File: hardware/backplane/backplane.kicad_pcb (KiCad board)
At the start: 4 copper layers, 192 x 31.5 mm, 83 parts, among them J1 Bus_PCI_Express_x1, J2 PWR, J3 Bus_PCI_Express_x1, J4 Bus_PCI_Express_x1, J5 Bus_PCI_Express_x1, J6 Bus_PCI_Express_x1, J7 Bus_PCI_Express_x1, J8 Bus_PCI_Express_x1, M1 FAN1, Q1 IRFS7530TRL7PP, Q2 AO3400A, U1 TPS5430DDA, U2 TCA9548APWR, U3 TCA9539PWR, U4 LM74700

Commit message: chore(backplane): fix 3d models
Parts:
- D10, D5, D6, D7, D8, D9: footprint LED_SMD:LED_WS2812B-2020_PLCC4_2.0x2.0mm -> Local Library:LED_WS2812B-2020_PLCC4_2.0x2.0mm

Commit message: chore: assembly cleanup
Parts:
- D10, D5, D6, D7, D8, D9: value WS2812C-2020 -> WS2812C-2020-V6

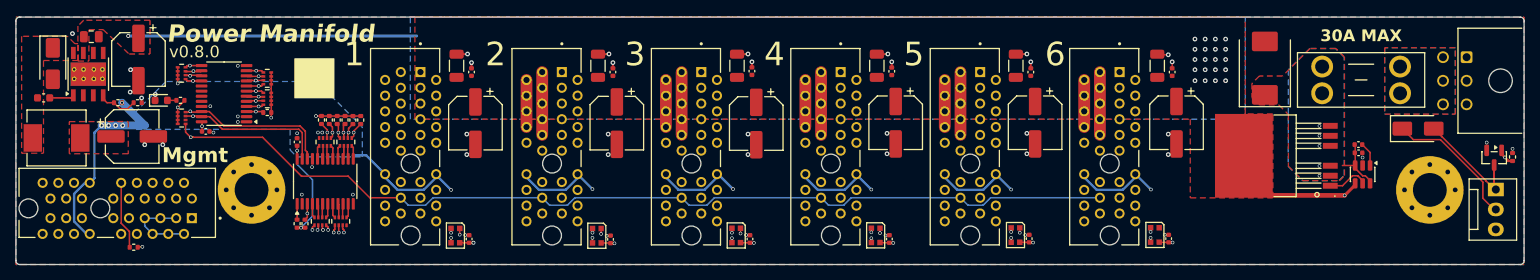
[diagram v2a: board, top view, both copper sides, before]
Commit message: feat(backplane): update pcb for higher power
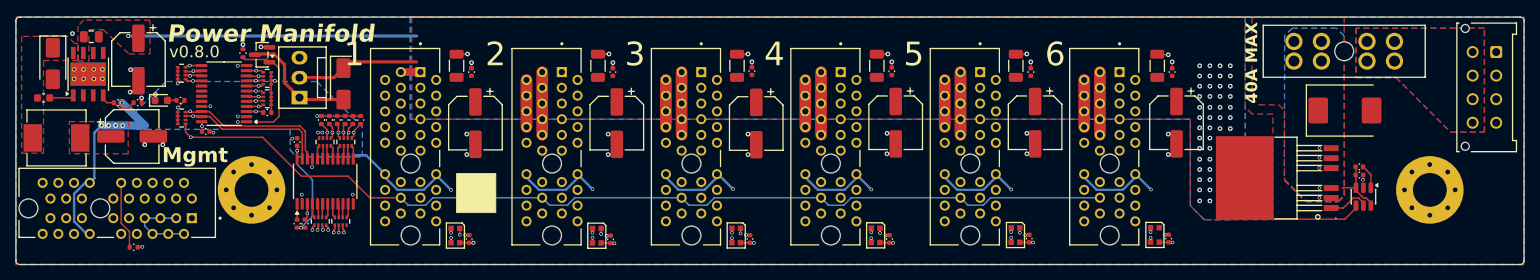
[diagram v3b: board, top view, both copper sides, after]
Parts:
- F1: value 20A -> 40A; footprint Local Library:Fuseholder_Blade_Mini_Keystone_3568 -> Local Library:FuseHolder_Blade_ATO_Littelfuse_FLR_178.6165
- J2: footprint Local Library:Molex_Micro-Fit_3.0_43045-0600_2x03_P3.00mm_Horizontal -> Local Library:Molex_Micro-Fit_3.0_43045-0812_2x04_P3.00mm_Vertical
- moved R8 162.2 mm to (63.9, 54.6)
- moved Q2 157.4 mm to (66.3, 54.8), turned to 180 degrees
- moved M1 152.7 mm to (71.1, 60.2), turned to 90 degrees
- moved D4 136.9 mm to (76.7, 58.5), turned to -90 degrees
- moved D1 11.5 mm to (204.2, 61.9), turned to 0 degrees
- moved F1 4.81 mm to (197.7, 53.1)
- moved J2 3.83 mm to (223.4, 54.5)
- moved Q1 2.83 mm to (196.9, 70.5)
- moved C8 2.83 mm to (206.0, 69.1)
- moved U4 2.83 mm to (206.6, 72.9)
- moved C6 2.83 mm to (206.0, 70.1)
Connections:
- J2 pad 4: /VIN_PREFUSE -> GND
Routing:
- net /FAN: track 159.9 -> 34.2 mm
- net VIN: track 124.2 -> 99.2 mm, vias 22 -> 43
- net /SCL4: track 86.6 -> 90.3 mm
- net /SCL3: track 68.8 -> 72.1 mm
- net GND: track 83.0 -> 85.5 mm
- net Net-(D4-A): track 17.5 -> 15.1 mm
- net /LED_DATA: track 43.7 -> 41.3 mm
- net /SDA4: track 79.6 -> 81.9 mm
- net /SDA3: track 60.6 -> 62.7 mm
- net /SCL2: track 49.1 -> 50.6 mm
- net /SCL1: track 29.9 -> 31.4 mm
- net /SDA2: track 41.5 -> 43.0 mm
- net /SDA1: track 22.7 -> 24.1 mm
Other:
- board text added: "40A MAX"
- board text removed: "30A MAX"
